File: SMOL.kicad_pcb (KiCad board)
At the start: 2 copper layers, 12.7 x 14.2 mm, 13 parts, among them Q1 Q_NMOS_GSD, U1 TLV61220, U2 ATTINY13-20SSU

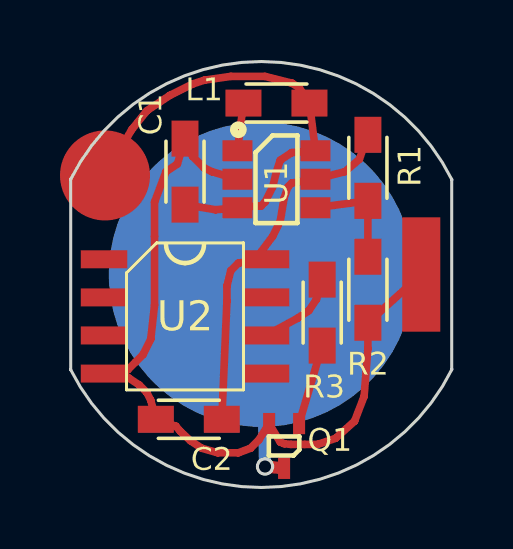
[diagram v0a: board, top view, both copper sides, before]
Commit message: Hacky fix to board outline; fixed Q1's 3d representation
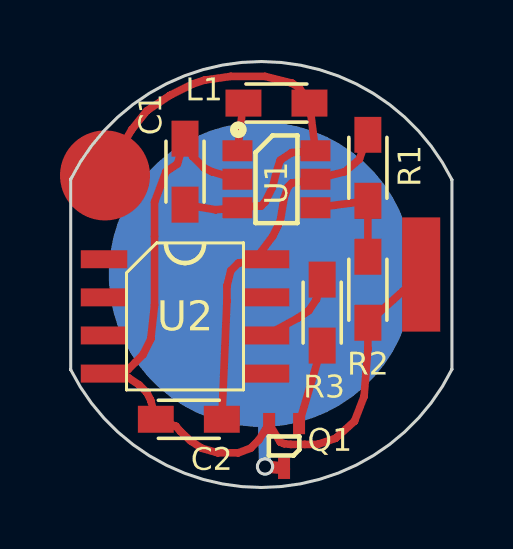
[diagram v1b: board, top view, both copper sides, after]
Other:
- rule pad_to_mask_clearance: 0.2 -> 0.1524
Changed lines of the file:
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@@
     (links 19)
     (no_connects 0)
-    (area 80.935962 94.449683 108.007994 109.042201)
+    (area 95.199199 94.449683 108.007994 108.750317)
     (thickness 1.6)
     (drawings 4)
@@
     (pad_size 1.2 0.9)
     (pad_drill 0)
-    (pad_to_mask_clearance 0.2)
+    (pad_to_mask_clearance 0.1524)
     (aux_axis_origin 0 0)
     (visible_elements 7FFFFF7F)
@@
       (net 3 /μC_Vcc))
     (model ${KISYS3DMOD}/TO_SOT_Packages_SMD.3dshapes/SuperSOT-6.wrl
-      (at (xyz 0 0 0))
-      (scale (xyz 1 1 1))
-      (rotate (xyz 0 0 0))
-    )
-  )
-  (module SMOL_footprints:SOT523_HandSoldering (layer F.Cu)
-    (at 102.362 107.315 180)
-    (descr "3-pin TSOT23 package, http://www.analog.com.tw/pdf/All_In_One.pdf")
-    (tags TSOT-23)
-    (attr smd)
-    (fp_text reference Q1 (at -1.524 0.1905 180) (layer F.SilkS)
-      (effects (font (size 0.762 0.762) (thickness 0.1524)))
-    )
-    (fp_text value Q_NMOS_GSD (at 16.256 3.937 180) (layer F.Fab) hide
-      (effects (font (size 1 1) (thickness 0.15)))
-    )
-    (fp_line (start 0.508 0.3175) (end -0.508 0.3175) (layer F.SilkS) (width 0.1524))
-    (fp_line (start -0.508 0.3175) (end -0.508 -0.127) (layer F.SilkS) (width 0.1524))
-    (fp_line (start -0.508 -0.127) (end -0.3175 -0.3175) (layer F.SilkS) (width 0.1524))
-    (fp_line (start -0.3175 -0.3175) (end 0.508 -0.3175) (layer F.SilkS) (width 0.1524))
-    (fp_line (start 0.508 -0.3175) (end 0.508 0.3175) (layer F.SilkS) (width 0.1524))
-    (fp_line (start -1.016 1.397) (end -1.016 -1.397) (layer F.CrtYd) (width 0.0508))
-    (fp_line (start -1.016 1.397) (end 1.016 1.397) (layer F.CrtYd) (width 0.0508))
-    (fp_line (start 1.016 -1.397) (end -1.016 -1.397) (layer F.CrtYd) (width 0.0508))
-    (fp_line (start 1.016 -1.397) (end 1.016 1.397) (layer F.CrtYd) (width 0.0508))
-    (pad 1 smd rect (at -0.5 0.745 180) (size 0.4 0.71) (layers F.Cu F.Mask)
-      (net 5 "Net-(Q1-Pad1)"))
-    (pad 2 smd rect (at 0.5 0.745 180) (size 0.4 0.71) (layers F.Cu F.Mask)
-      (net 2 /Anode))
-    (pad 3 smd rect (at 0 -0.745 180) (size 0.4 0.71) (layers F.Cu F.Mask)
-      (net 6 /Spring_Contact))
-    (model ${KISYS3DMOD}/TO_SOT_Packages_SMD.3dshapes/TSOT-23.wrl
       (at (xyz 0 0 0))
       (scale (xyz 1 1 1))
@@
       (xy -4.163414 5.010811) (xy -4.127292 5.059803) (xy -4.086971 5.098791) (xy -4.056051 5.096233)) (layer B.SilkS) (width 0.01))
   )
-  (gr_line (start 107.95 104.775) (end 107.95 98.425) (angle 90) (layer Edge.Cuts) (width 0.1016))
+  (module SMOL_footprints:SOT523_HandSoldering (layer F.Cu)
+    (at 102.362 107.315 180)
+    (descr "3-pin TSOT23 package, http://www.analog.com.tw/pdf/All_In_One.pdf")
+    (tags TSOT-23)
+    (attr smd)
+    (fp_text reference Q1 (at -1.524 0.1905 180) (layer F.SilkS)
+      (effects (font (size 0.762 0.762) (thickness 0.1524)))
+    )
+    (fp_text value Q_NMOS_GSD (at 16.256 3.937 180) (layer F.Fab) hide
+      (effects (font (size 1 1) (thickness 0.15)))
+    )
+    (fp_line (start 0.508 0.3175) (end -0.508 0.3175) (layer F.SilkS) (width 0.1524))
+    (fp_line (start -0.508 0.3175) (end -0.508 -0.127) (layer F.SilkS) (width 0.1524))
+    (fp_line (start -0.508 -0.127) (end -0.3175 -0.3175) (layer F.SilkS) (width 0.1524))
+    (fp_line (start -0.3175 -0.3175) (end 0.508 -0.3175) (layer F.SilkS) (width 0.1524))
+    (fp_line (start 0.508 -0.3175) (end 0.508 0.3175) (layer F.SilkS) (width 0.1524))
+    (fp_line (start -1.016 1.397) (end -1.016 -1.397) (layer F.CrtYd) (width 0.0508))
+    (fp_line (start -1.016 1.397) (end 1.016 1.397) (layer F.CrtYd) (width 0.0508))
+    (fp_line (start 1.016 -1.397) (end -1.016 -1.397) (layer F.CrtYd) (width 0.0508))
+    (fp_line (start 1.016 -1.397) (end 1.016 1.397) (layer F.CrtYd) (width 0.0508))
+    (pad 1 smd rect (at -0.5 0.745 180) (size 0.4 0.71) (layers F.Cu F.Mask)
+      (net 5 "Net-(Q1-Pad1)"))
+    (pad 2 smd rect (at 0.5 0.745 180) (size 0.4 0.71) (layers F.Cu F.Mask)
+      (net 2 /Anode))
+    (pad 3 smd rect (at 0 -0.745 180) (size 0.4 0.71) (layers F.Cu F.Mask)
+      (net 6 /Spring_Contact))
+    (model TO_SOT_Packages_SMD.3dshapes/SOT-23.wrl
+      (at (xyz 0 0 0))
+      (scale (xyz 0.5 0.5 0.5))
+      (rotate (xyz 0 0 -90))
+    )
+  )
+  (gr_line (start 107.957193 104.760573) (end 107.957193 98.439427) (angle 90) (layer Edge.Cuts) (width 0.1016))
   (gr_line (start 95.25 104.775) (end 95.25 98.425) (angle 90) (layer Edge.Cuts) (width 0.1016))
   (gr_arc (start 101.6 101.6) (end 95.25 104.775) (angle -127) (layer Edge.Cuts) (width 0.1016))
